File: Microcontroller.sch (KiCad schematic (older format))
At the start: 35 parts

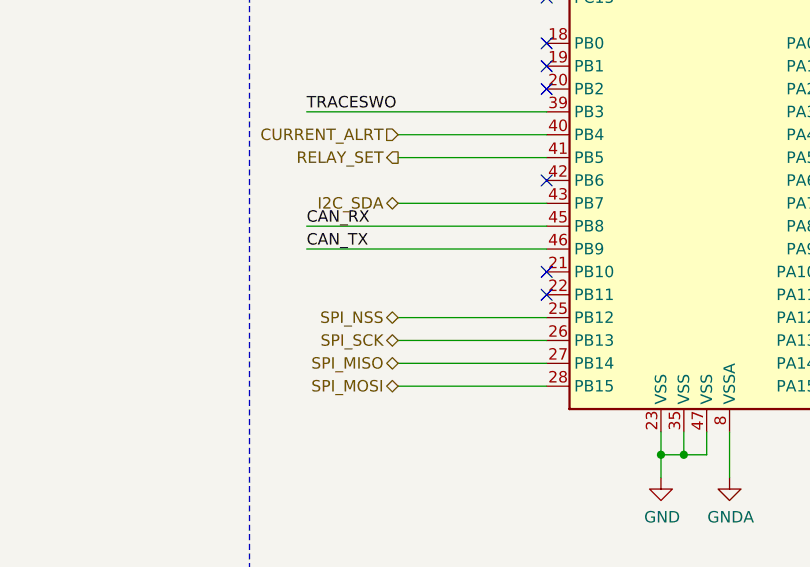
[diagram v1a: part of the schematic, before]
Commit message: Added display driver for 7 segment
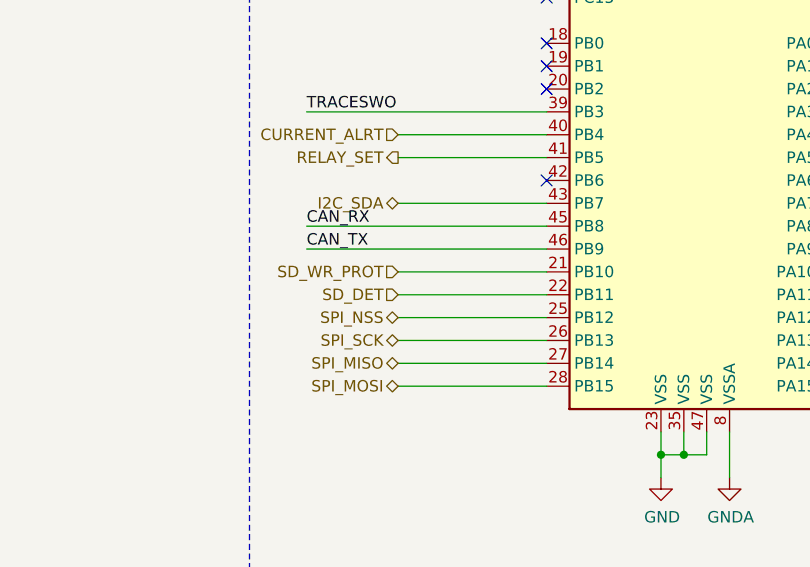
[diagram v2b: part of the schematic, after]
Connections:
- net SD_WR_PROT: now reaches U?.21 (PB10)
- net SD_DET: now reaches U?.22 (PB11)
- no-connect marks 12 -> 10
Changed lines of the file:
@@
 $Descr A4 11693 8268
 encoding utf-8
-Sheet 1 7
+Sheet 2 7
 Title ""
 Date ""
@@
 Text Label 5150 2200 2    50   ~ 0
 LEDS
-NoConn ~ 8500 5250
-NoConn ~ 8500 5150
 NoConn ~ 8500 4350
 NoConn ~ 8500 4250
@@
 NoConn ~ 8500 3850
 NoConn ~ 8500 4750
+Wire Wire Line
+	8500 5150 7850 5150
+Text HLabel 7850 5150 0    50   Input ~ 0
+SD_WR_PROT
+Wire Wire Line
+	8500 5250 7850 5250
+Text HLabel 7850 5250 0    50   Input ~ 0
+SD_DET
 Wire Bus Line
 	10400 4650 10400 5150

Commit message: Done with preliminary schematic. Needs review
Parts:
- R201, R202, R205, R206, R207, R209, R210, R211: renamed from R?; footprint (none) -> Resistor_SMD:R_0603_1608Metric
- R203, R204, R208: renamed from R?; footprint (none) -> Resistor_SMD:R_0201_0603Metric
- gave numbers to parts that had none: 24
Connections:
- net SW1: now reaches U201.18 (PB0)
- net SW2: now reaches U201.19 (PB1)
- net SW3: now reaches U201.20 (PB2)
- no-connect marks 10 -> 7

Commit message: Added stuff
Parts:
- D201, D202, D203, D204, D205, D206: footprint (none) -> LED_SMD:LED_0603_1608Metric
- SW201: value SW_Push -> B3U-1100P
- U202: footprint (none) -> Package_SO:SOIC-8_3.9x4.9mm_P1.27mm
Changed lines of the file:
@@
 F 0 "U202" H 1900 7200 50  0000 C CNN
 F 1 "NCV7357" H 1500 7200 50  0000 C CNN
-F 2 "" H 1550 7000 50  0001 C CNN
+F 2 "Package_SO:SOIC-8_3.9x4.9mm_P1.27mm" H 1550 7000 50  0001 C CNN
 F 3 "" H 1550 7000 50  0001 C CNN
 	1    1650 6800
@@
 P 1200 3450
 F 0 "SW201" H 1200 3643 50  0000 C CNN
-F 1 "SW_Push" H 1200 3644 50  0001 C CNN
+F 1 "B3U-1100P " H 1200 3644 50  0001 C CNN
 F 2 "" H 1200 3650 50  0001 C CNN
 F 3 "~" H 1200 3650 50  0001 C CNN
@@
 F 0 "D205" H 4150 4000 50  0000 R CNN
 F 1 "LED" H 4000 3700 50  0001 R CNN
-F 2 "" H 4100 3900 50  0001 C CNN
+F 2 "LED_SMD:LED_0603_1608Metric" H 4100 3900 50  0001 C CNN
 F 3 "~" H 4100 3900 50  0001 C CNN
 	1    4100 3900
@@
 F 0 "D201" H 4093 2425 50  0000 C CNN
 F 1 "LED" V 4048 2182 50  0001 R CNN
-F 2 "" H 4100 2300 50  0001 C CNN
+F 2 "LED_SMD:LED_0603_1608Metric" H 4100 2300 50  0001 C CNN
 F 3 "~" H 4100 2300 50  0001 C CNN
 	1    4100 2300
@@
 F 0 "D202" H 4093 2825 50  0000 C CNN
 F 1 "LED" V 4048 2582 50  0001 R CNN
-F 2 "" H 4100 2700 50  0001 C CNN
+F 2 "LED_SMD:LED_0603_1608Metric" H 4100 2700 50  0001 C CNN
 F 3 "~" H 4100 2700 50  0001 C CNN
 	1    4100 2700
@@
 F 0 "D203" H 4093 3225 50  0000 C CNN
 F 1 "LED" V 4048 2982 50  0001 R CNN
-F 2 "" H 4100 3100 50  0001 C CNN
+F 2 "LED_SMD:LED_0603_1608Metric" H 4100 3100 50  0001 C CNN
 F 3 "~" H 4100 3100 50  0001 C CNN
 	1    4100 3100
@@
 F 0 "D204" H 4150 3600 50  0000 R CNN
 F 1 "LED" H 4000 3300 50  0001 R CNN
-F 2 "" H 4100 3500 50  0001 C CNN
+F 2 "LED_SMD:LED_0603_1608Metric" H 4100 3500 50  0001 C CNN
 F 3 "~" H 4100 3500 50  0001 C CNN
 	1    4100 3500
@@
 F 0 "D206" H 4100 4250 50  0000 C CNN
 F 1 "LED" H 3900 4450 50  0001 C CNN
-F 2 "" H 4100 4350 50  0001 C CNN
+F 2 "LED_SMD:LED_0603_1608Metric" H 4100 4350 50  0001 C CNN
 F 3 "~" H 4100 4350 50  0001 C CNN
 	1    4100 4350

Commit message: Done with footprints
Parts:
- J201: footprint (none) -> ReflowOven:CNC_3221-10-0100-00
- SW201: footprint (none) -> ReflowOven:SW_B3U-1100P
- X201: footprint (none) -> ReflowOven:KC2016Z48.0000C15XXK
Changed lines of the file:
@@
 F 0 "X201" H 1775 5115 50  0000 C CNN
 F 1 "OSC_4PIN" H 1775 5024 50  0000 C CNN
-F 2 "" V 1750 4750 50  0001 C CNN
+F 2 "ReflowOven:KC2016Z48.0000C15XXK" V 1750 4750 50  0001 C CNN
 F 3 "" V 1750 4750 50  0001 C CNN
 	1    1800 4750
@@
 F 0 "J201" H 1450 2225 50  0000 C CNN
 F 1 "Conn_02x05_Counter_Clockwise" H 1450 2226 50  0001 C CNN
-F 2 "" H 1400 1900 50  0001 C CNN
+F 2 "ReflowOven:CNC_3221-10-0100-00" H 1400 1900 50  0001 C CNN
 F 3 "~" H 1400 1900 50  0001 C CNN
 	1    1400 1900
@@
 F 0 "SW201" H 1200 3643 50  0000 C CNN
 F 1 "B3U-1100P " H 1200 3644 50  0001 C CNN
-F 2 "" H 1200 3650 50  0001 C CNN
+F 2 "ReflowOven:SW_B3U-1100P" H 1200 3650 50  0001 C CNN
 F 3 "~" H 1200 3650 50  0001 C CNN
 	1    1200 3450

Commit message: Began routing
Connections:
- net +3.3VA is gone; now on net +3V3: U201.9 (VDDA)
- net SW_BTN: now reaches U201.42 (PB6)
- net USB_DM renamed USB_D-
- net USB_DP renamed USB_D+
- no-connect marks 7 -> 6
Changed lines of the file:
@@
 Wire Wire Line
 	9300 6050 9300 5850
-Wire Wire Line
-	9400 2850 9400 2550
-$Comp
-L power:+3.3VA #PWR0204
-U 1 1 5F65932B
-P 9400 2550
-F 0 "#PWR0204" H 9400 2400 50  0001 C CNN
-F 1 "+3.3VA" H 9415 2723 50  0000 C CNN
-F 2 "" H 9400 2550 50  0001 C CNN
-F 3 "" H 9400 2550 50  0001 C CNN
-	1    9400 2550
-	1    0    0    -1
-$EndComp
 $Comp
 L power:+3V3 #PWR0223
@@
 I2C_SCL
 Text HLabel 10600 5250 2    50   BiDi ~ 0
-USB_DP
+USB_D+
 Text HLabel 10600 5350 2    50   BiDi ~ 0
-USB_DM
+USB_D-
 Wire Wire Line
 	7850 4550 8500 4550
@@
 NoConn ~ 8500 3950
 NoConn ~ 8500 3850
-NoConn ~ 8500 4750
 Wire Wire Line
 	8500 5150 7850 5150
@@
 Text HLabel 7850 4250 0    50   Input Italic 0
 SW2
+Wire Wire Line
+	8500 4750 7850 4750
+Text HLabel 7850 4750 0    50   Input Italic 0
+SW_BTN
+Wire Wire Line
+	9300 2700 9400 2700
+Wire Wire Line
+	9400 2700 9400 2850
 Wire Bus Line
 	10400 4650 10400 5150
 Wire Bus Line
 	4750 2200 4750 4450
+Connection ~ 9300 2700
 $EndSCHEMATC

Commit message: Footprint update
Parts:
- removed J201: Conn_02x05_Counter_Clockwise, ReflowOven:CNC_3221-10-0100-00, symbol Connector_Generic:Conn_02x05_Counter_Clockwise
- added J201: Conn_02x05_Odd_Even, ReflowOven:CNC_3221-10-0100-00, symbol Connector_Generic:Conn_02x05_Odd_Even
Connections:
- net +3V3: now also J201.1 (Pin_1)
- net GND: now also J201.3 (Pin_3), J201.5 (Pin_5), J201.9 (Pin_9)
- net SWDCLK: now also J201.4 (Pin_4)
- net SWDIO: now also J201.2 (Pin_2)
- net TRACESWO: now also J201.6 (Pin_6)
- net ~RST: now also J201.10 (Pin_10)
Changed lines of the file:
@@
 	500  4200 2800 4200
 NoConn ~ 8500 3550
-$Comp
-L Connector_Generic:Conn_02x05_Counter_Clockwise J201
-U 1 1 5F82EAA8
-P 1400 1900
-F 0 "J201" H 1450 2225 50  0000 C CNN
-F 1 "Conn_02x05_Counter_Clockwise" H 1450 2226 50  0001 C CNN
-F 2 "ReflowOven:CNC_3221-10-0100-00" H 1400 1900 50  0001 C CNN
-F 3 "~" H 1400 1900 50  0001 C CNN
-	1    1400 1900
-	1    0    0    -1
-$EndComp
 Wire Wire Line
 	1200 1700 1100 1700
@@
 	4750 2200 4750 4450
 Connection ~ 9300 2700
+$Comp
+L Connector_Generic:Conn_02x05_Odd_Even J201
+U 1 1 5FA30A37
+P 1400 1900
+F 0 "J201" H 1450 2225 50  0000 C CNN
+F 1 "Conn_02x05_Odd_Even" H 1450 2226 50  0001 C CNN
+F 2 "ReflowOven:CNC_3221-10-0100-00" H 1400 1900 50  0001 C CNN
+F 3 "~" H 1400 1900 50  0001 C CNN
+	1    1400 1900
+	1    0    0    -1
+$EndComp
 $EndSCHEMATC

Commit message: Done for today with layout
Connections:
- net CANH: no longer U202.7 (CANH)
- net CANL: no longer U202.6 (CANL)
- new net CAN+: U202.7 (CANH)
- new net CAN-: U202.6 (CANL)
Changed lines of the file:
@@
 	1100 6550 1250 6550
 Text HLabel 900  6850 0    50   BiDi ~ 0
-CANL
+CAN-
 $Comp
 L power:+3V3 #PWR0219
@@
 	1250 7000 1200 7000
 Text HLabel 900  6700 0    50   BiDi ~ 0
-CANH
+CAN+
 $Comp
 L power:GND #PWR0231
